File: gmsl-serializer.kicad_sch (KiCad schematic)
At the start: 6 parts

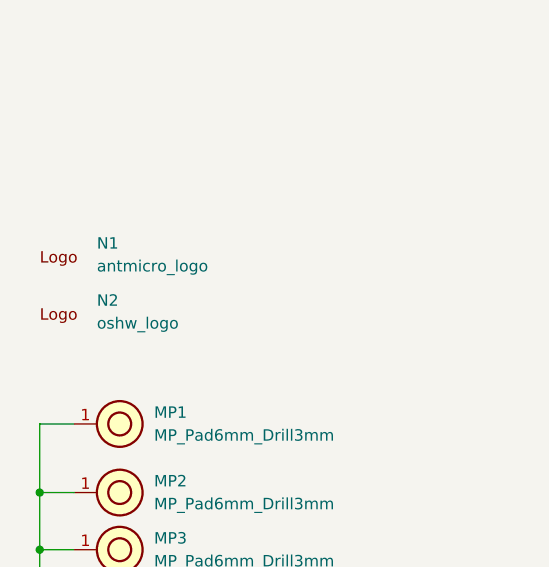
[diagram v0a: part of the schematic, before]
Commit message: [#55438] Add LED indicators to schematics
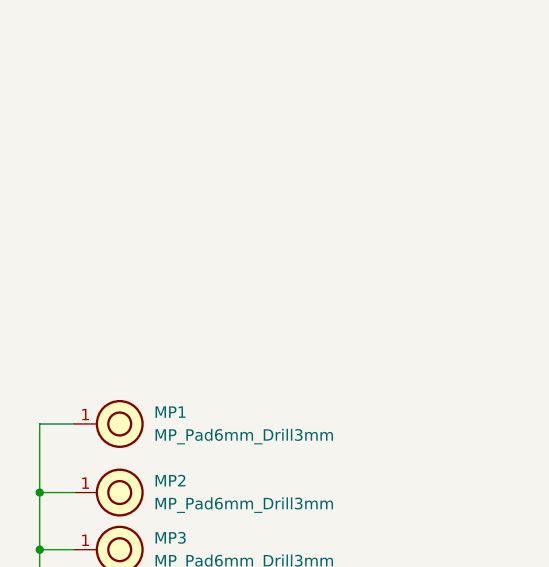
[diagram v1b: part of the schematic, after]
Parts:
- removed N1: antmicro_logo, antmicro-footprints:antmicro-logo_scaled_12mm, symbol antmicroMechanicalParts:antmicro_logo
- removed N2: oshw_logo, antmicro-footprints:oshw-logo, symbol antmicroMechanicalParts:oshw_logo

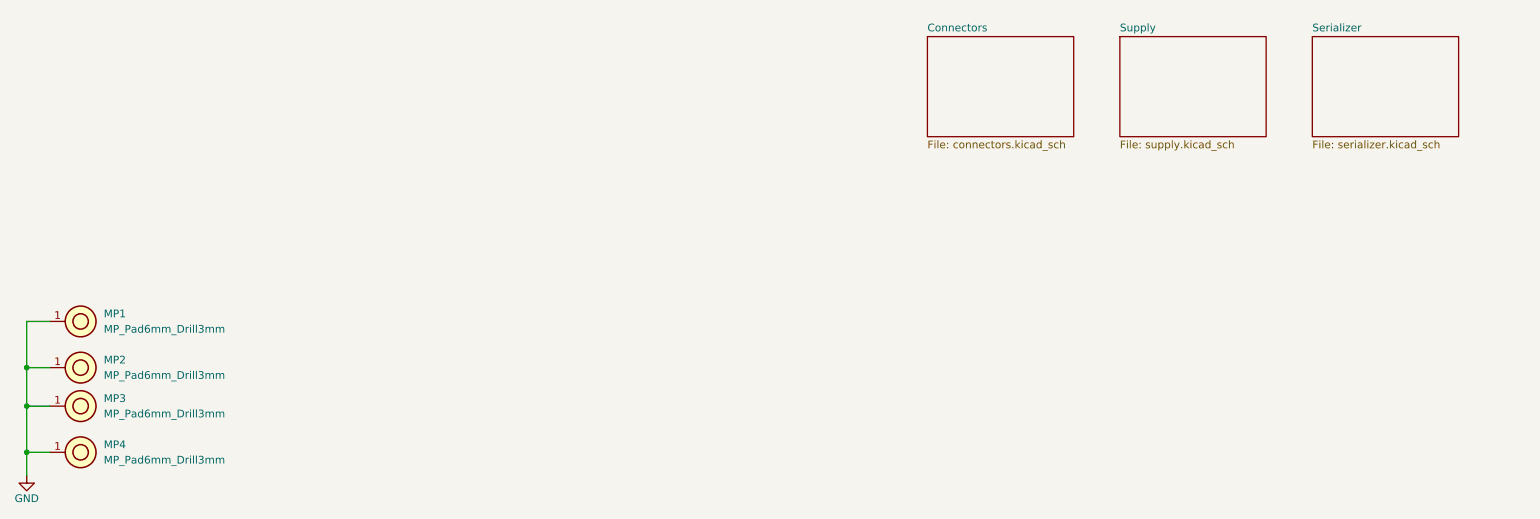
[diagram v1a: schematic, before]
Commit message: [#55438] Place LED indicators on PCB
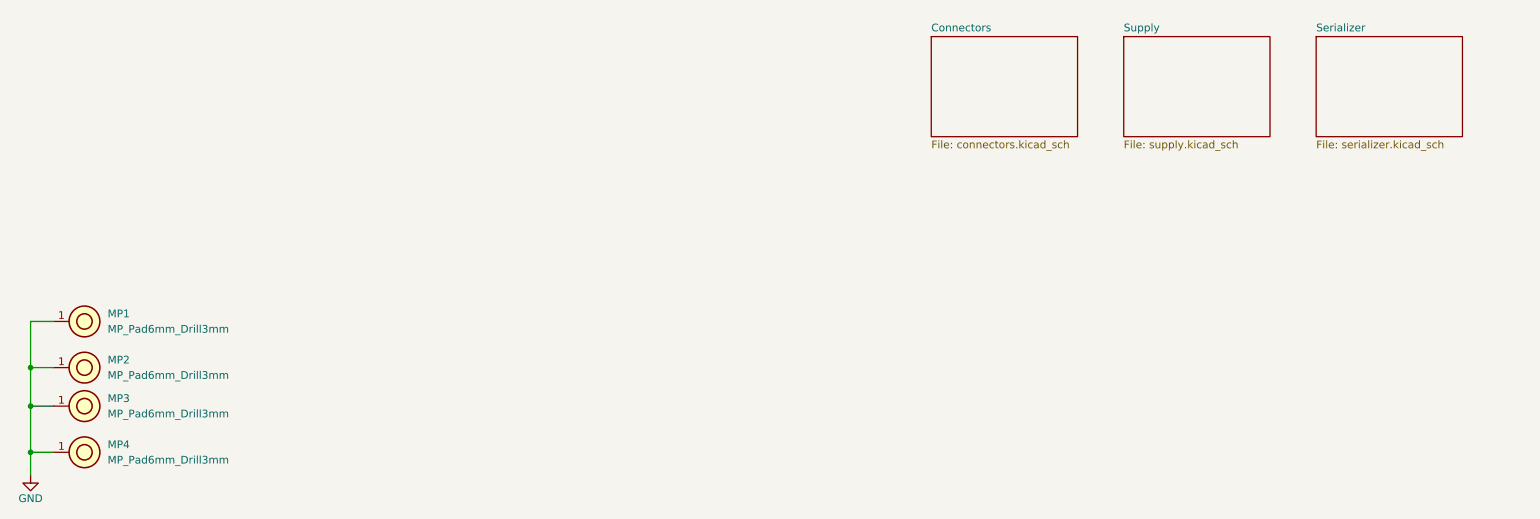
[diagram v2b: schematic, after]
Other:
- moved on the sheet: MP1, MP2, MP3, MP4

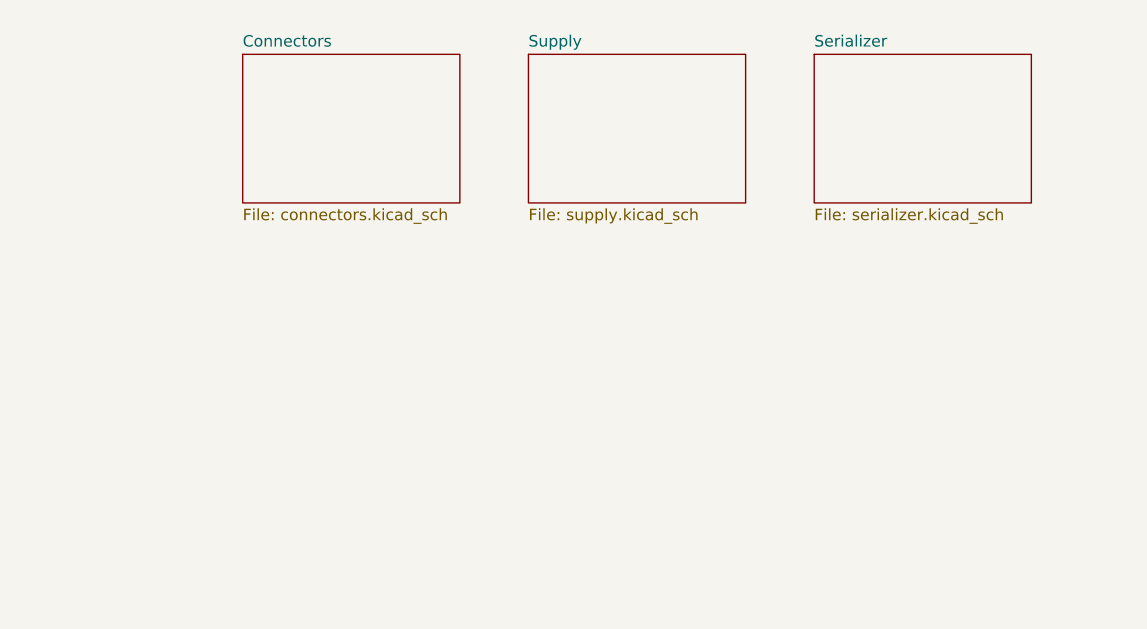
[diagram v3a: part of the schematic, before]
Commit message: [#66847] Make schematic hierarchical
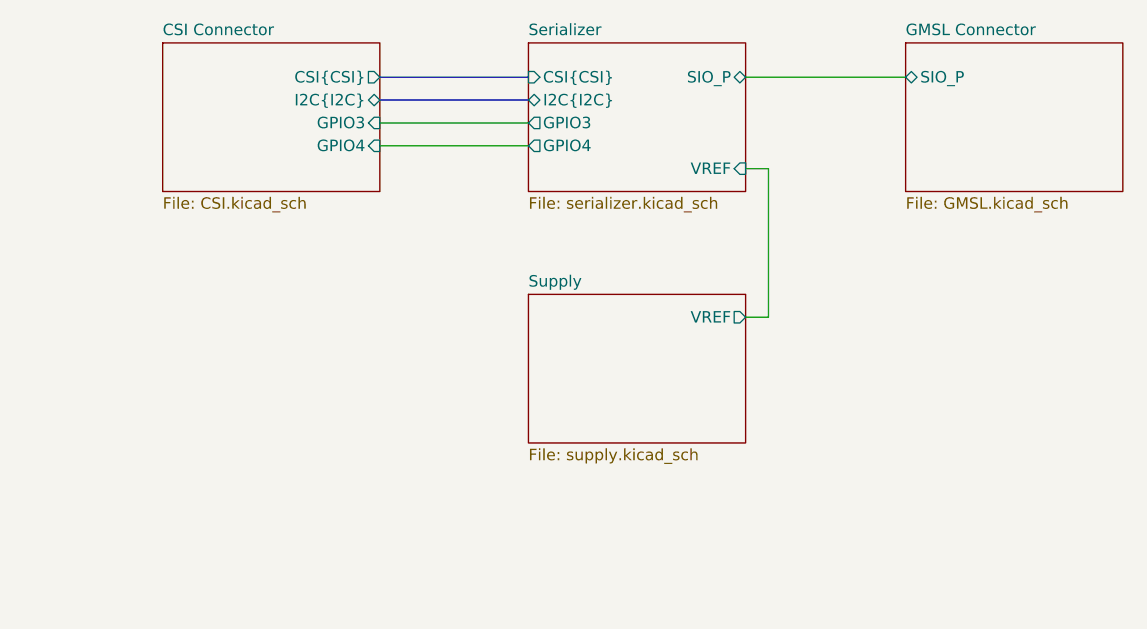
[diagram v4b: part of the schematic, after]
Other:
- sheet Connectors renamed CSI Connector
- added sheet GMSL Connector (GMSL.kicad_sch)
- sheet CSI Connector: file connectors.kicad_sch -> CSI.kicad_sch
- sheet CSI Connector ports: added CSI{CSI}, GPIO3, GPIO4, I2C{I2C}; removed none
- sheet Serializer ports: added CSI{CSI}, GPIO3, GPIO4, I2C{I2C}, SIO_P, VREF; removed none
- sheet Supply ports: added VREF; removed none
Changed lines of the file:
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@@
   (junction (at 27.94 232.41) (diameter 0) (color 0 0 0 0)
   )
+  (wire (pts (xy 234.95 184.15) (xy 232.41 184.15))
+    (stroke (width 0) (type default))
+  )
+  (wire (pts (xy 234.95 200.66) (xy 234.95 184.15))
+    (stroke (width 0) (type default))
+  )
+  (wire (pts (xy 232.41 200.66) (xy 234.95 200.66))
+    (stroke (width 0) (type default))
+  )
   (wire (pts (xy 31.75 218.44) (xy 27.94 218.44))
     (stroke (width 0) (type default))
@@
     (stroke (width 0) (type default))
   )
+  (bus (pts (xy 191.77 173.99) (xy 208.28 173.99))
+    (stroke (width 0) (type default))
+  )
   (wire (pts (xy 27.94 218.44) (xy 27.94 226.06))
     (stroke (width 0) (type default))
   )
+  (wire (pts (xy 232.41 173.99) (xy 250.19 173.99))
+    (stroke (width 0) (type default))
+  )
+  (wire (pts (xy 191.77 181.61) (xy 208.28 181.61))
+    (stroke (width 0) (type default))
+  )
   (wire (pts (xy 27.94 226.06) (xy 27.94 232.41))
     (stroke (width 0) (type default))
   )
+  (bus (pts (xy 191.77 176.53) (xy 208.28 176.53))
+    (stroke (width 0) (type default))
+  )
   (wire (pts (xy 31.75 240.03) (xy 27.94 240.03))
     (stroke (width 0) (type default))
@@
     (stroke (width 0) (type default))
   )
+  (wire (pts (xy 191.77 179.07) (xy 208.28 179.07))
+    (stroke (width 0) (type default))
+  )
   (wire (pts (xy 27.94 232.41) (xy 27.94 240.03))
     (stroke (width 0) (type default))
@@
     )
   )
-  (sheet (at 176.53 171.45) (size 24.13 16.51) (fields_autoplaced)
+  (sheet (at 250.19 170.18) (size 24.13 16.51) (fields_autoplaced)
     (stroke (width 0.1524) (type solid))
     (fill (color 0 0 0 0.0000))
-    (property "Sheetname" "Connectors" (at 176.53 170.7384 0)
+    (property "Sheetname" "GMSL Connector" (at 250.19 169.4684 0)
       (effects (font (size 1.27 1.27)) (justify left bottom))
     )
-    (property "Sheetfile" "connectors.kicad_sch" (at 176.53 188.5446 0)
+    (property "Sheetfile" "GMSL.kicad_sch" (at 250.19 187.2746 0)
       (effects (font (size 1.27 1.27)) (justify left top))
     )
+    (pin "SIO_P" bidirectional (at 250.19 173.99 180)
+      (effects (font (size 1.27 1.27)) (justify left))
+    )
+    (instances
+      (project "gmsl-serializer"
+        (path "/dbd1044a-3803-4c19-8db2-96636cba7198" (page "5"))
+      )
+    )
+  )
+  (sheet (at 167.64 170.18) (size 24.13 16.51) (fields_autoplaced)
+    (stroke (width 0.1524) (type solid))
+    (fill (color 0 0 0 0.0000))
+    (property "Sheetname" "CSI Connector" (at 167.64 169.4684 0)
+      (effects (font (size 1.27 1.27)) (justify left bottom))
+    )
+    (property "Sheetfile" "CSI.kicad_sch" (at 167.64 187.2746 0)
+      (effects (font (size 1.27 1.27)) (justify left top))
+    )
+    (pin "CSI{CSI}" output (at 191.77 173.99 0)
+      (effects (font (size 1.27 1.27)) (justify right))
+    )
+    (pin "I2C{I2C}" bidirectional (at 191.77 176.53 0)
+      (effects (font (size 1.27 1.27)) (justify right))
+    )
+    (pin "GPIO4" input (at 191.77 181.61 0)
+      (effects (font (size 1.27 1.27)) (justify right))
+    )
+    (pin "GPIO3" input (at 191.77 179.07 0)
+      (effects (font (size 1.27 1.27)) (justify right))
+    )
     (instances
       (project "gmsl-serializer"
@@
     )
   )
-  (sheet (at 240.03 171.45) (size 24.13 16.51) (fields_autoplaced)
+  (sheet (at 208.28 170.18) (size 24.13 16.51) (fields_autoplaced)
     (stroke (width 0.1524) (type solid))
     (fill (color 0 0 0 0.0000))
-    (property "Sheetname" "Serializer" (at 240.03 170.7384 0)
+    (property "Sheetname" "Serializer" (at 208.28 169.4684 0)
       (effects (font (size 1.27 1.27)) (justify left bottom))
     )
-    (property "Sheetfile" "serializer.kicad_sch" (at 240.03 188.5446 0)
+    (property "Sheetfile" "serializer.kicad_sch" (at 208.28 187.2746 0)
       (effects (font (size 1.27 1.27)) (justify left top))
     )
+    (pin "GPIO4" output (at 208.28 181.61 180)
+      (effects (font (size 1.27 1.27)) (justify left))
+    )
+    (pin "GPIO3" output (at 208.28 179.07 180)
+      (effects (font (size 1.27 1.27)) (justify left))
+    )
+    (pin "VREF" input (at 232.41 184.15 0)
+      (effects (font (size 1.27 1.27)) (justify right))
+    )
+    (pin "I2C{I2C}" bidirectional (at 208.28 176.53 180)
+      (effects (font (size 1.27 1.27)) (justify left))
+    )
+    (pin "SIO_P" bidirectional (at 232.41 173.99 0)
+      (effects (font (size 1.27 1.27)) (justify right))
+    )
+    (pin "CSI{CSI}" input (at 208.28 173.99 180)
+      (effects (font (size 1.27 1.27)) (justify left))
+    )
     (instances
       (project "gmsl-serializer"
@@
     )
   )
-  (sheet (at 208.28 171.45) (size 24.13 16.51) (fields_autoplaced)
+  (sheet (at 208.28 198.12) (size 24.13 16.51) (fields_autoplaced)
     (stroke (width 0.1524) (type solid))
     (fill (color 0 0 0 0.0000))
-    (property "Sheetname" "Supply" (at 208.28 170.7384 0)
+    (property "Sheetname" "Supply" (at 208.28 197.4084 0)
       (effects (font (size 1.27 1.27)) (justify left bottom))
     )
-    (property "Sheetfile" "supply.kicad_sch" (at 208.28 188.5446 0)
+    (property "Sheetfile" "supply.kicad_sch" (at 208.28 215.2146 0)
       (effects (font (size 1.27 1.27)) (justify left top))
     )
+    (pin "VREF" output (at 232.41 200.66 0)
+      (effects (font (size 1.27 1.27)) (justify right))
+    )
     (instances

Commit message: [#66847] Update DNP style; Update from lib; Fix CSI bus definition
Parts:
- MP1, MP2, MP3, MP4: now left out of the parts list
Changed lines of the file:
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@@
   )
   (symbol (lib_id "antmicroMechanicalParts:MP_Pad6mm_Drill3mm") (at 31.75 240.03 0) (unit 1)
-    (in_bom yes) (on_board yes) (dnp no) (fields_autoplaced)
+    (in_bom no) (on_board yes) (dnp no) (fields_autoplaced)
     (property "Reference" "MP4" (at 40.64 238.7599 0)
       (effects (font (size 1.27 1.27) (thickness 0.15)) (justify left))
@@
   )
   (symbol (lib_id "antmicroMechanicalParts:MP_Pad6mm_Drill3mm") (at 31.75 218.44 0) (unit 1)
-    (in_bom yes) (on_board yes) (dnp no) (fields_autoplaced)
+    (in_bom no) (on_board yes) (dnp no) (fields_autoplaced)
     (property "Reference" "MP1" (at 40.64 217.1699 0)
       (effects (font (size 1.27 1.27) (thickness 0.15)) (justify left))
@@
   )
   (symbol (lib_id "antmicroMechanicalParts:MP_Pad6mm_Drill3mm") (at 31.75 226.06 0) (unit 1)
-    (in_bom yes) (on_board yes) (dnp no) (fields_autoplaced)
+    (in_bom no) (on_board yes) (dnp no) (fields_autoplaced)
     (property "Reference" "MP2" (at 40.64 224.7899 0)
       (effects (font (size 1.27 1.27) (thickness 0.15)) (justify left))
@@
   )
   (symbol (lib_id "antmicroMechanicalParts:MP_Pad6mm_Drill3mm") (at 31.75 232.41 0) (unit 1)
-    (in_bom yes) (on_board yes) (dnp no) (fields_autoplaced)
+    (in_bom no) (on_board yes) (dnp no) (fields_autoplaced)
     (property "Reference" "MP3" (at 40.64 231.1399 0)
       (effects (font (size 1.27 1.27) (thickness 0.15)) (justify left))
